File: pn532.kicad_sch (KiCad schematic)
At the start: 1 part

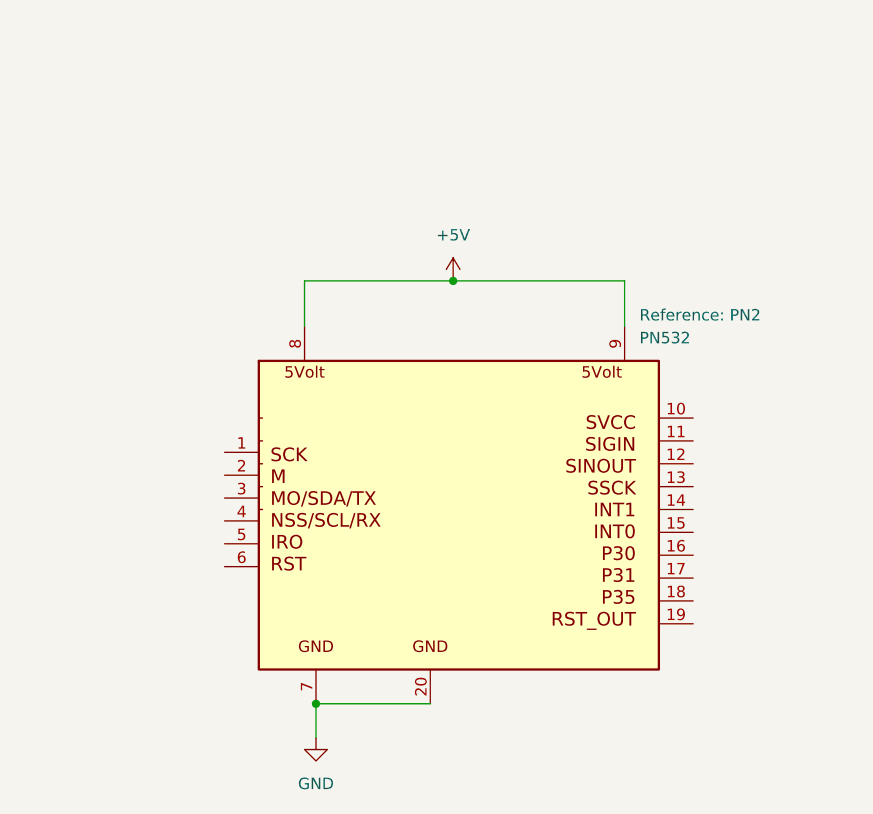
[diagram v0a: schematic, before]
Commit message: Add hierarchical labels for ALL PN532 pins (22 pins, _PN532 suffix)
Each pin of PN2 now has a hierarchical label with name matching the pin
plus _PN532 suffix (e.g. SCK_PN532, INT_PN532, GND_PN532)
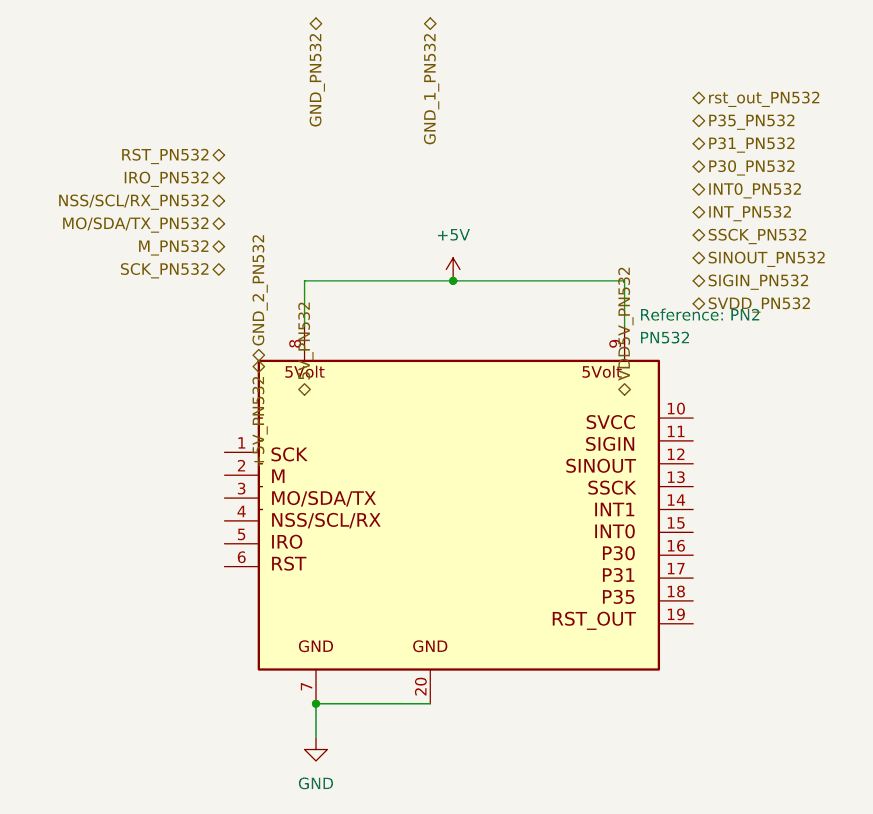
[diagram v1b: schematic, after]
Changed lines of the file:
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@@
 		)
 	)
-	(symbol
+		(symbol
 		(lib_id "power:+5V")
 		(at 162.56 63.5 0)
@@
 		)
 	)
+	(hierarchical_label "+5V_PN532"
+		(shape bidirectional)
+		(at 140.97 72.39 270)
+		(effects
+			(font
+				(size 1.27 1.27)
+			)
+		)
+	)
+	(hierarchical_label "5V_PN532"
+		(shape bidirectional)
+		(at 146.05 76.20 90)
+		(effects
+			(font
+				(size 1.27 1.27)
+			)
+		)
+	)
+	(hierarchical_label "GND_PN532"
+		(shape bidirectional)
+		(at 147.32 34.29 270)
+		(effects
+			(font
+				(size 1.27 1.27)
+			)
+		)
+	)
+	(hierarchical_label "GND_1_PN532"
+		(shape bidirectional)
+		(at 160.02 34.29 270)
+		(effects
+			(font
+				(size 1.27 1.27)
+			)
+		)
+	)
+	(hierarchical_label "GND_2_PN532"
+		(shape bidirectional)
+		(at 140.97 72.39 90)
+		(effects
+			(font
+				(size 1.27 1.27)
+			)
+		)
+	)
+	(hierarchical_label "INT_PN532"
+		(shape bidirectional)
+		(at 189.23 55.88 0)
+		(effects
+			(font
+				(size 1.27 1.27)
+			)
+			(justify left)
+		)
+	)
+	(hierarchical_label "INT0_PN532"
+		(shape bidirectional)
+		(at 189.23 53.34 0)
+		(effects
+			(font
+				(size 1.27 1.27)
+			)
+			(justify left)
+		)
+	)
+	(hierarchical_label "IRO_PN532"
+		(shape bidirectional)
+		(at 137.16 52.07 180)
+		(effects
+			(font
+				(size 1.27 1.27)
+			)
+			(justify right)
+		)
+	)
+	(hierarchical_label "M_PN532"
+		(shape bidirectional)
+		(at 137.16 59.69 180)
+		(effects
+			(font
+				(size 1.27 1.27)
+			)
+			(justify right)
+		)
+	)
+	(hierarchical_label "MO/SDA/TX_PN532"
+		(shape bidirectional)
+		(at 137.16 57.15 180)
+		(effects
+			(font
+				(size 1.27 1.27)
+			)
+			(justify right)
+		)
+	)
+	(hierarchical_label "NSS/SCL/RX_PN532"
+		(shape bidirectional)
+		(at 137.16 54.61 180)
+		(effects
+			(font
+				(size 1.27 1.27)
+			)
+			(justify right)
+		)
+	)
+	(hierarchical_label "P30_PN532"
+		(shape bidirectional)
+		(at 189.23 50.80 0)
+		(effects
+			(font
+				(size 1.27 1.27)
+			)
+			(justify left)
+		)
+	)
+	(hierarchical_label "P31_PN532"
+		(shape bidirectional)
+		(at 189.23 48.26 0)
+		(effects
+			(font
+				(size 1.27 1.27)
+			)
+			(justify left)
+		)
+	)
+	(hierarchical_label "P35_PN532"
+		(shape bidirectional)
+		(at 189.23 45.72 0)
+		(effects
+			(font
+				(size 1.27 1.27)
+			)
+			(justify left)
+		)
+	)
+	(hierarchical_label "RST_PN532"
+		(shape bidirectional)
+		(at 137.16 49.53 180)
+		(effects
+			(font
+				(size 1.27 1.27)
+			)
+			(justify right)
+		)
+	)
+	(hierarchical_label "SCK_PN532"
+		(shape bidirectional)
+		(at 137.16 62.23 180)
+		(effects
+			(font
+				(size 1.27 1.27)
+			)
+			(justify right)
+		)
+	)
+	(hierarchical_label "SIGIN_PN532"
+		(shape bidirectional)
+		(at 189.23 63.50 0)
+		(effects
+			(font
+				(size 1.27 1.27)
+			)
+			(justify left)
+		)
+	)
+	(hierarchical_label "SINOUT_PN532"
+		(shape bidirectional)
+		(at 189.23 60.96 0)
+		(effects
+			(font
+				(size 1.27 1.27)
+			)
+			(justify left)
+		)
+	)
+	(hierarchical_label "SSCK_PN532"
+		(shape bidirectional)
+		(at 189.23 58.42 0)
+		(effects
+			(font
+				(size 1.27 1.27)
+			)
+			(justify left)
+		)
+	)
+	(hierarchical_label "SVDD_PN532"
+		(shape bidirectional)
+		(at 189.23 66.04 0)
+		(effects
+			(font
+				(size 1.27 1.27)
+			)
+			(justify left)
+		)
+	)
+	(hierarchical_label "VDD5V_PN532"
+		(shape bidirectional)
+		(at 181.61 76.20 90)
+		(effects
+			(font
+				(size 1.27 1.27)
+			)
+		)
+	)
+	(hierarchical_label "rst_out_PN532"
+		(shape bidirectional)
+		(at 189.23 43.18 0)
+		(effects
+			(font
+				(size 1.27 1.27)
+			)
+			(justify left)
+		)
+	)

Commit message: Remove all GND hierarchical pins and labels from all sheets
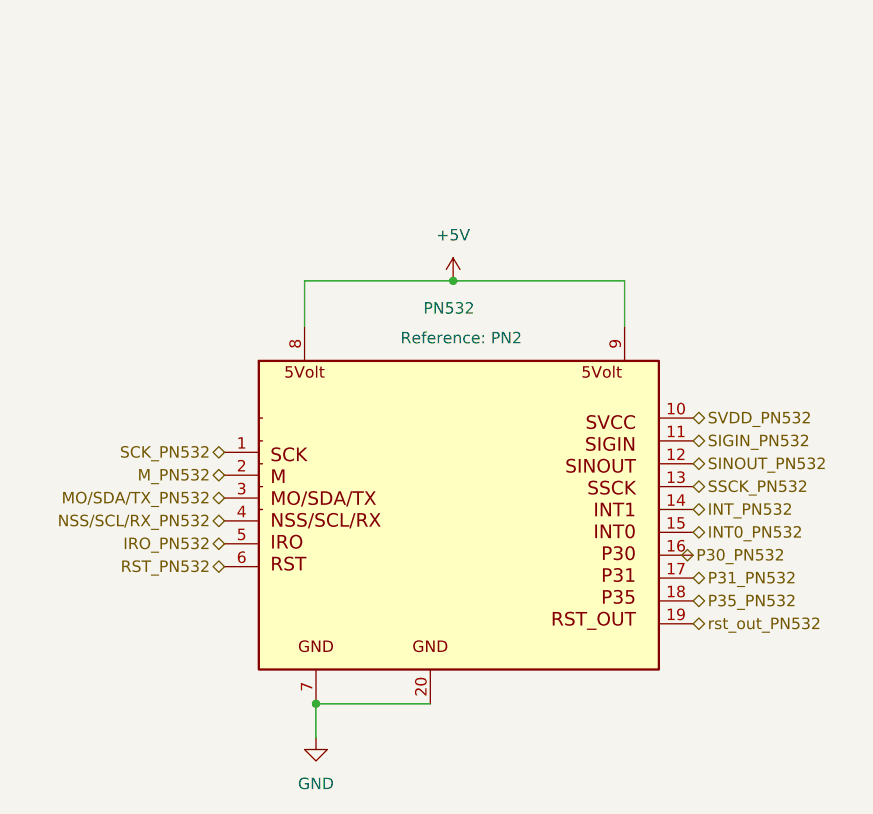
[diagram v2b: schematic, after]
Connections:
- net INT0_PN532: now also PN2.15 (INT0)
- net INT_PN532: now also PN2.14 (INT)
- net IRO_PN532: now also PN2.5 (IRO)
- net MO/SDA/TX_PN532: now also PN2.3 (MO/SDA/TX)
- net M_PN532: now also PN2.2 (M)
- net NSS/SCL/RX_PN532: now also PN2.4 (NSS/SCL/RX)
- net P31_PN532: now also PN2.17 (P31)
- net P35_PN532: now also PN2.18 (P35)
- net RST_PN532: now also PN2.6 (RST)
- net SCK_PN532: now also PN2.1 (SCK)
- net SIGIN_PN532: now also PN2.11 (SIGIN)
- net SINOUT_PN532: now also PN2.12 (SINOUT)
- net SSCK_PN532: now also PN2.13 (SSCK)
- net SVDD_PN532: now also PN2.10 (SVDD)
- net rst_out_PN532: now also PN2.19 (rst_out)
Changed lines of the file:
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@@
 		)
 	)
-		(symbol
+	(hierarchical_label "SSCK_PN532"
+		(shape bidirectional)
+		(at 189.23 86.36 0)
+		(effects
+			(font
+				(size 1.27 1.27)
+			)
+			(justify left)
+		)
+	)
+	(hierarchical_label "INT0_PN532"
+		(shape bidirectional)
+		(at 189.23 91.44 0)
+		(effects
+			(font
+				(size 1.27 1.27)
+			)
+			(justify left)
+		)
+	)
+	(hierarchical_label "SVDD_PN532"
+		(shape bidirectional)
+		(at 189.23 78.74 0)
+		(effects
+			(font
+				(size 1.27 1.27)
+			)
+			(justify left)
+		)
+	)
+	(hierarchical_label "NSS/SCL/RX_PN532"
+		(shape bidirectional)
+		(at 137.16 90.17 180)
+		(effects
+			(font
+				(size 1.27 1.27)
+			)
+			(justify right)
+		)
+	)
+	(hierarchical_label "IRO_PN532"
+		(shape bidirectional)
+		(at 137.16 92.71 180)
+		(effects
+			(font
+				(size 1.27 1.27)
+			)
+			(justify right)
+		)
+	)
+	(hierarchical_label "P30_PN532"
+		(shape bidirectional)
+		(at 187.96 93.98 0)
+		(effects
+			(font
+				(size 1.27 1.27)
+			)
+			(justify left)
+		)
+	)
+	(hierarchical_label "M_PN532"
+		(shape bidirectional)
+		(at 137.16 85.09 180)
+		(effects
+			(font
+				(size 1.27 1.27)
+			)
+			(justify right)
+		)
+	)
+	(hierarchical_label "P31_PN532"
+		(shape bidirectional)
+		(at 189.23 96.52 0)
+		(effects
+			(font
+				(size 1.27 1.27)
+			)
+			(justify left)
+		)
+	)
+	(hierarchical_label "SINOUT_PN532"
+		(shape bidirectional)
+		(at 189.23 83.82 0)
+		(effects
+			(font
+				(size 1.27 1.27)
+			)
+			(justify left)
+		)
+	)
+	(hierarchical_label "P35_PN532"
+		(shape bidirectional)
+		(at 189.23 99.06 0)
+		(effects
+			(font
+				(size 1.27 1.27)
+			)
+			(justify left)
+		)
+	)
+	(hierarchical_label "MO/SDA/TX_PN532"
+		(shape bidirectional)
+		(at 137.16 87.63 180)
+		(effects
+			(font
+				(size 1.27 1.27)
+			)
+			(justify right)
+		)
+	)
+	(hierarchical_label "SCK_PN532"
+		(shape bidirectional)
+		(at 137.16 82.55 180)
+		(effects
+			(font
+				(size 1.27 1.27)
+			)
+			(justify right)
+		)
+	)
+	(hierarchical_label "rst_out_PN532"
+		(shape bidirectional)
+		(at 189.23 101.6 0)
+		(effects
+			(font
+				(size 1.27 1.27)
+			)
+			(justify left)
+		)
+	)
+	(hierarchical_label "SIGIN_PN532"
+		(shape bidirectional)
+		(at 189.23 81.28 0)
+		(effects
+			(font
+				(size 1.27 1.27)
+			)
+			(justify left)
+		)
+	)
+	(hierarchical_label "RST_PN532"
+		(shape bidirectional)
+		(at 137.16 95.25 180)
+		(effects
+			(font
+				(size 1.27 1.27)
+			)
+			(justify right)
+		)
+	)
+	(hierarchical_label "INT_PN532"
+		(shape bidirectional)
+		(at 189.23 88.9 0)
+		(effects
+			(font
+				(size 1.27 1.27)
+			)
+			(justify left)
+		)
+	)
+	(symbol
 		(lib_id "power:+5V")
 		(at 162.56 63.5 0)
@@
 		(in_pos_files yes)
 		(dnp no)
-		(fields_autoplaced yes)
 		(property "Reference" "PN2"
-			(at 183.2611 67.31 0)
+			(at 156.718 69.85 0)
 			(show_name yes)
 			(do_not_autoplace no)
@@
 		)
 		(property "Value" "PN532"
-			(at 183.2611 69.85 0)
+			(at 159.258 66.548 0)
 			(show_name no)
 			(do_not_autoplace no)
@@
 		)
 	)
-	(hierarchical_label "+5V_PN532"
-		(shape bidirectional)
-		(at 140.97 72.39 270)
-		(effects
-			(font
-				(size 1.27 1.27)
-			)
-		)
-	)
-	(hierarchical_label "5V_PN532"
-		(shape bidirectional)
-		(at 146.05 76.20 90)
-		(effects
-			(font
-				(size 1.27 1.27)
-			)
-		)
-	)
-	(hierarchical_label "GND_PN532"
-		(shape bidirectional)
-		(at 147.32 34.29 270)
-		(effects
-			(font
-				(size 1.27 1.27)
-			)
-		)
-	)
-	(hierarchical_label "GND_1_PN532"
-		(shape bidirectional)
-		(at 160.02 34.29 270)
-		(effects
-			(font
-				(size 1.27 1.27)
-			)
-		)
-	)
-	(hierarchical_label "GND_2_PN532"
-		(shape bidirectional)
-		(at 140.97 72.39 90)
-		(effects
-			(font
-				(size 1.27 1.27)
-			)
-		)
-	)
-	(hierarchical_label "INT_PN532"
-		(shape bidirectional)
-		(at 189.23 55.88 0)
-		(effects
-			(font
-				(size 1.27 1.27)
-			)
-			(justify left)
-		)
-	)
-	(hierarchical_label "INT0_PN532"
-		(shape bidirectional)
-		(at 189.23 53.34 0)
-		(effects
-			(font
-				(size 1.27 1.27)
-			)
-			(justify left)
-		)
-	)
-	(hierarchical_label "IRO_PN532"
-		(shape bidirectional)
-		(at 137.16 52.07 180)
-		(effects
-			(font
-				(size 1.27 1.27)
-			)
-			(justify right)
-		)
-	)
-	(hierarchical_label "M_PN532"
-		(shape bidirectional)
-		(at 137.16 59.69 180)
-		(effects
-			(font
-				(size 1.27 1.27)
-			)
-			(justify right)
-		)
-	)
-	(hierarchical_label "MO/SDA/TX_PN532"
-		(shape bidirectional)
-		(at 137.16 57.15 180)
-		(effects
-			(font
-				(size 1.27 1.27)
-			)
-			(justify right)
-		)
-	)
-	(hierarchical_label "NSS/SCL/RX_PN532"
-		(shape bidirectional)
-		(at 137.16 54.61 180)
-		(effects
-			(font
-				(size 1.27 1.27)
-			)
-			(justify right)
-		)
-	)
-	(hierarchical_label "P30_PN532"
-		(shape bidirectional)
-		(at 189.23 50.80 0)
-		(effects
-			(font
-				(size 1.27 1.27)
-			)
-			(justify left)
-		)
-	)
-	(hierarchical_label "P31_PN532"
-		(shape bidirectional)
-		(at 189.23 48.26 0)
-		(effects
-			(font
-				(size 1.27 1.27)
-			)
-			(justify left)
-		)
-	)
-	(hierarchical_label "P35_PN532"
-		(shape bidirectional)
-		(at 189.23 45.72 0)
-		(effects
-			(font
-				(size 1.27 1.27)
-			)
-			(justify left)
-		)
-	)
-	(hierarchical_label "RST_PN532"
-		(shape bidirectional)
-		(at 137.16 49.53 180)
-		(effects
-			(font
-				(size 1.27 1.27)
-			)
-			(justify right)
-		)
-	)
-	(hierarchical_label "SCK_PN532"
-		(shape bidirectional)
-		(at 137.16 62.23 180)
-		(effects
-			(font
-				(size 1.27 1.27)
-			)
-			(justify right)
-		)
-	)
-	(hierarchical_label "SIGIN_PN532"
-		(shape bidirectional)
-		(at 189.23 63.50 0)
-		(effects
-			(font
-				(size 1.27 1.27)
-			)
-			(justify left)
-		)
-	)
-	(hierarchical_label "SINOUT_PN532"
-		(shape bidirectional)
-		(at 189.23 60.96 0)
-		(effects
-			(font
-				(size 1.27 1.27)
-			)
-			(justify left)
-		)
-	)
-	(hierarchical_label "SSCK_PN532"
-		(shape bidirectional)
-		(at 189.23 58.42 0)
-		(effects
-			(font
-				(size 1.27 1.27)
-			)
-			(justify left)
-		)
-	)
-	(hierarchical_label "SVDD_PN532"
-		(shape bidirectional)
-		(at 189.23 66.04 0)
-		(effects
-			(font
-				(size 1.27 1.27)
-			)
-			(justify left)
-		)
-	)
-	(hierarchical_label "VDD5V_PN532"
-		(shape bidirectional)
-		(at 181.61 76.20 90)
-		(effects
-			(font
-				(size 1.27 1.27)
-			)
-		)
-	)
-	(hierarchical_label "rst_out_PN532"
-		(shape bidirectional)
-		(at 189.23 43.18 0)
-		(effects
-			(font
-				(size 1.27 1.27)
-			)
-			(justify left)
-		)
-	)

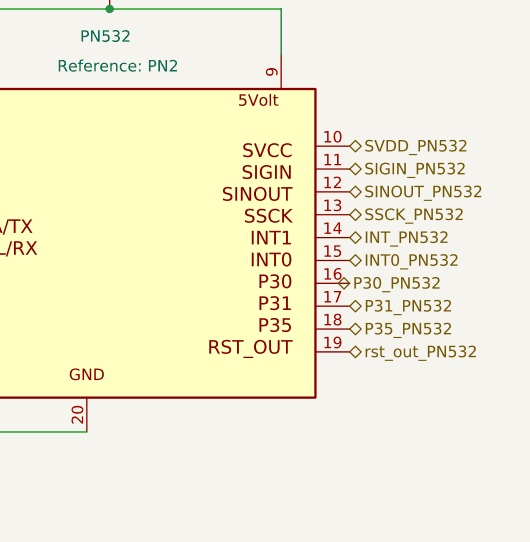
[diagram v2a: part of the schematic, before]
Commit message: Add hierarchical labels/pins across all sheets, fix DiscoveryAnalog3 rename, PCB 99x99mm rounded corners
- nfc_rpi.kicad_sch: 19 hierarchical pins on PN532 sheet
- pn532.kicad_sch: 22 hierarchical labels with _PN532 suffix
- raspberry_pn532.kicad_sch: 68 hierarchical labels for J1
- nfc.kicad_sch: 54 signal pins on Raspberry sheet, power pins removed
- switch.kicad_sch: 8 switch+resistor circuits with hierarchical labels
- oled.kicad_sch: 7 hierarchical labels
- DiscoveryAnalog3.kicad_sch: 26 hierarchical labels for J4 connector
- nfc_rpi.kicad_pcb: 99x99mm board outline with 5mm rounded corners (gr_line + gr_arc)
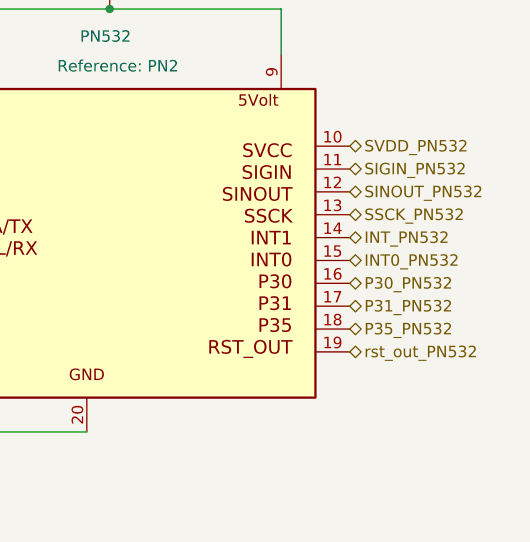
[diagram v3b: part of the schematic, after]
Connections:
- net P30_PN532: now also PN2.16 (P30)
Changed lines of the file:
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@@
 	(hierarchical_label "P30_PN532"
 		(shape bidirectional)
-		(at 187.96 93.98 0)
+		(at 189.23 93.98 0)
 		(effects
 			(font
